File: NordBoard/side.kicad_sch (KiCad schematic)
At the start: 39 parts, among them SW15 SW_Push, SW16 SW_Push, SW2 SW_Push, SW22 SW_Push, SW23 SW_Push, SW24 SW_Push, SW25 SW_Push, SW26 SW_Push, SW27 SW_Push, SW28 SW_Push, SW29 SW_Push, SW30 SW_Push, SW31 SW_Push, SW32 SW_Push, SW33 SW_Push, SW34 SW_Push, SW9 SW_Push, U1 MOUDLE-SEEEDUINO-XIAO

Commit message: feat: finish schem, finish PCB layout
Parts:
- removed U1: MOUDLE-SEEEDUINO-XIAO, Seeed Studio XIAO Series Library:XIAO-RP2040-DIP, symbol XIAO_RP2040:MOUDLE-SEEEDUINO-XIAO
- added U2: Seeeduino Xiao rp2040, PCM_marbastlib-xp-promicroish:Xiao_rp2040_ACH, symbol PCM_marbastlib-promicroish:Seeeduino_Xiao_rp2040
- D1, D19, D20, D21, D22, D23, D24, D25, D26, D27, D28, D29, D30, D31, D32, D33, D34: footprint (none) -> Diode_SMD:D_SMA-SMB_Universal_Handsoldering
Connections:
- net COL0: now also U2.2 (P27)
- net COL1: now also U2.3 (P28)
- net COL2: now also U2.4 (P29)
- net COL3: now also SW30.1, U2.5 (P6)
- net COL4: now also U2.6 (P7)
- net GND: now also U2.9 (GND)
- net ROW0: now also U2.11 (P3)
- net ROW1: now also U2.12 (P4)
- net ROW2: now also U2.13 (P2)
- net ROW3: now also U2.14 (P1)
- no-connect marks 4 -> 10
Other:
- note added: "Matrix Left"
- note added: "Xiao"

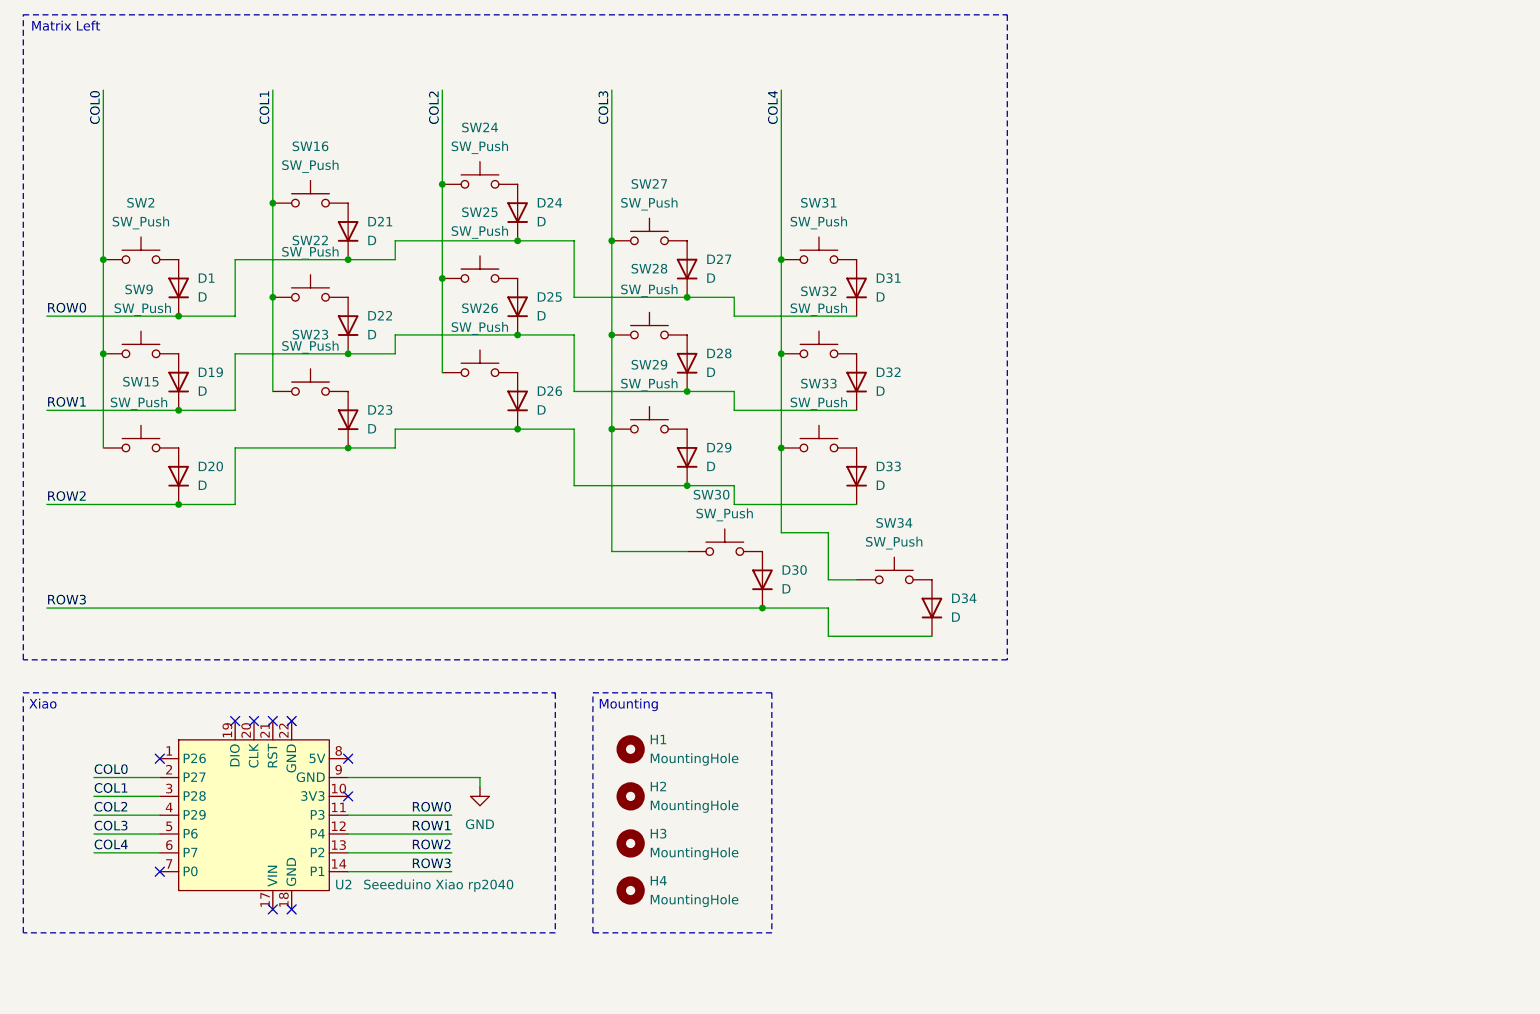
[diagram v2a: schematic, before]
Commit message: feat: new col in schem (not in PCB)
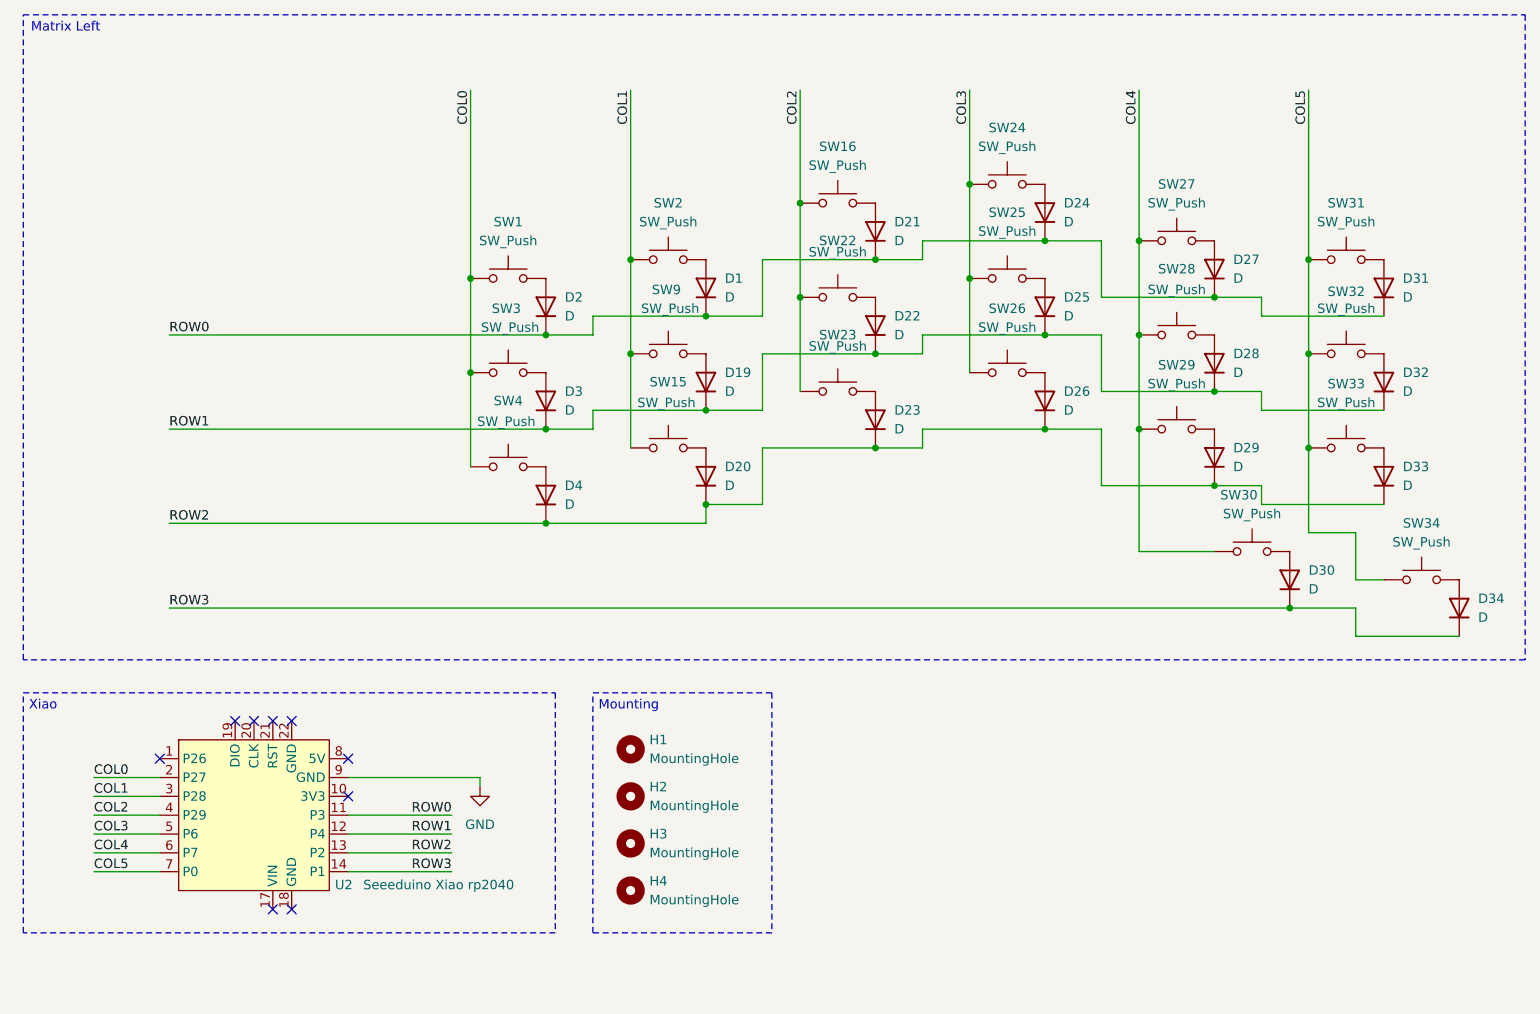
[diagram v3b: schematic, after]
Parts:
- added D2, D3, D4: D, Diode_SMD:D_SMA-SMB_Universal_Handsoldering, symbol Device:D
- added SW1, SW3, SW4: SW_Push, PCM_marbastlib-choc:SW_choc_v1_1u, symbol Switch:SW_Push
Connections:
- net COL0: now also SW1.1, SW3.1, SW4.1; no longer SW15.1, SW2.1, SW9.1
- net COL1: now also SW15.1, SW2.1, SW9.1; no longer SW16.1, SW22.1, SW23.1
- net COL2: now also SW16.1, SW22.1, SW23.1; no longer SW24.1, SW25.1, SW26.1
- net COL3: now also SW24.1, SW25.1, SW26.1; no longer SW27.1, SW28.1, SW29.1, SW30.1
- net COL4: now also SW27.1, SW28.1, SW29.1, SW30.1; no longer SW31.1, SW32.1, SW33.1, SW34.1
- net ROW0: now also D2.1 (K)
- net ROW1: now also D3.1 (K)
- net ROW2: now also D4.1 (K)
- net COL5: now reaches U2.7 (P0)
- net COL5: now also SW31.1, SW32.1, SW33.1, SW34.1
- new net: D3.2 (A), SW3.2
- new net: D4.2 (A), SW4.2
- new net: D2.2 (A), SW1.2
- no-connect marks 10 -> 9
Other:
- moved on the sheet: D1, D19, D20, D21, D22, D23, D24, D25, D26, D27, D28, D29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

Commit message: feat: revamp schem
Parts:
- removed U2: Seeeduino Xiao rp2040, PCM_marbastlib-xp-promicroish:Xiao_rp2040_ACH, symbol PCM_marbastlib-promicroish:Seeeduino_Xiao_rp2040
- added U1: XIAO-RP2040-DIP, Seeed Studio XIAO Series Library:XIAO-RP2040-DIP, symbol Seeed_Studio_XIAO_Series:XIAO-RP2040-DIP
- renumbered D2 to D1, D24 to D10, D25 to D11, D26 to D12, D27 to D13, D28 to D14, D29 to D15, D30 to D16, D31 to D17, D32 to D18, D33 to D19, D3 to D2, D34 to D20, D4 to D3, D1 to D4, D19 to D5, D20 to D6, D21 to D7, D22 to D8, D23 to D9, SW24 to SW10, SW25 to SW11, SW26 to SW12, SW27 to SW13, SW28 to SW14, SW29 to SW15, SW30 to SW16, SW31 to SW17, SW32 to SW18, SW33 to SW19, SW3 to SW2, SW34 to SW20, SW4 to SW3, SW2 to SW4, SW9 to SW5, SW15 to SW6, SW16 to SW7, SW22 to SW8, SW23 to SW9
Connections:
- net COL0: now also U1.2 (GPIO27/ADC1/A1)
- net COL1: now also U1.3 (GPIO28/ADC2/A2)
- net COL2: now also U1.4 (GPIO29/ADC3/A3)
- net COL3: now also U1.5 (GPIO6/SDA)
- net COL4: now also U1.6 (GPIO7/SCL)
- net COL5: now also U1.7 (GPIO0/TX)
- net GND: now also U1.13 (GND)
- net ROW0: now also U1.11 (GPIO3/MOSI)
- net ROW1: now also U1.10 (GPIO4/MISO)
- net ROW2: now also U1.9 (GPIO2/SCK)
- net ROW3: now also U1.8 (GPIO1/RX)
- no-connect marks 9 -> 3
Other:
- note added: "Matrix"
- note removed: "Matrix Left"
- moved on the sheet: D1, D10, D11, D12, D13, D14, D15, D16, D17, D18, D19, D2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

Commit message: chore: pcb board cleanup
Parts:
- removed H4: MountingHole, MountingHole:MountingHole_2.2mm_M2, symbol Mechanical:MountingHole
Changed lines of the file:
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@@
 	(rectangle
 		(start 101.6 110.49)
-		(end 125.73 142.875)
+		(end 125.73 135.89)
 		(stroke
 			(width 0)
@@
 				)
 				(path "/7cf7f72d-7ab1-4807-b592-339093d5ca44/a5832e99-b0f3-4441-a24d-2a862f25015f"
-					(reference "H5")
+					(reference "H4")
 					(unit 1)
 				)
@@
 	)
 	(symbol
-		(lib_id "Mechanical:MountingHole")
-		(at 106.68 137.16 0)
-		(unit 1)
-		(exclude_from_sim no)
-		(in_bom no)
-		(on_board yes)
-		(dnp no)
-		(fields_autoplaced yes)
-		(property "Reference" "H4"
-			(at 109.22 135.8899 0)
-			(effects
-				(font
-					(size 1.27 1.27)
-				)
-				(justify left)
-			)
-		)
-		(property "Value" "MountingHole"
-			(at 109.22 138.4299 0)
-			(effects
-				(font
-					(size 1.27 1.27)
-				)
-				(justify left)
-			)
-		)
-		(property "Footprint" "MountingHole:MountingHole_2.2mm_M2"
-			(at 106.68 137.16 0)
-			(effects
-				(font
-					(size 1.27 1.27)
-				)
-				(hide yes)
-			)
-		)
-		(property "Datasheet" "~"
-			(at 106.68 137.16 0)
-			(effects
-				(font
-					(size 1.27 1.27)
-				)
-				(hide yes)
-			)
-		)
-		(property "Description" "Mounting Hole without connection"
-			(at 106.68 137.16 0)
-			(effects
-				(font
-					(size 1.27 1.27)
-				)
-				(hide yes)
-			)
-		)
-		(instances
-			(project "NordBoard"
-				(path "/7cf7f72d-7ab1-4807-b592-339093d5ca44/7e48f610-41a3-4552-82fa-dd005ce074be"
-					(reference "H4")
-					(unit 1)
-				)
-				(path "/7cf7f72d-7ab1-4807-b592-339093d5ca44/a5832e99-b0f3-4441-a24d-2a862f25015f"
-					(reference "H8")
-					(unit 1)
-				)
-			)
-		)
-	)
-	(symbol
 		(lib_id "Switch:SW_Push")
 		(at 162.56 88.9 0)
@@
 				)
 				(path "/7cf7f72d-7ab1-4807-b592-339093d5ca44/a5832e99-b0f3-4441-a24d-2a862f25015f"
-					(reference "H6")
+					(reference "H5")
 					(unit 1)
 				)
@@
 				)
 				(path "/7cf7f72d-7ab1-4807-b592-339093d5ca44/a5832e99-b0f3-4441-a24d-2a862f25015f"
-					(reference "H7")
+					(reference "H6")
 					(unit 1)
 				)

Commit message: fix: fix pcb errors
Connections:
- net GND: no longer names the net of U1.13 (GND)
- no-connect marks 3 -> 4
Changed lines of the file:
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@@
 		(at 74.93 129.54)
 	)
+	(no_connect
+		(at 74.93 125.73)
+	)
 	(wire
 		(pts
@@
 	(wire
 		(pts
-			(xy 74.93 125.73) (xy 92.71 125.73)
-		)
-		(stroke
-			(width 0)
-			(type default)
-		)
-	)
-	(wire
-		(pts
 			(xy 142.24 80.01) (xy 157.48 80.01)
 		)
@@
 		(pts
 			(xy 74.93 144.78) (xy 88.9 144.78)
-		)
-		(stroke
-			(width 0)
-			(type default)
-		)
-	)
-	(wire
-		(pts
-			(xy 92.71 125.73) (xy 92.71 127)
 		)
 		(stroke
@@
 					(unit 1)
 				)
-			)
-		)
-	)
-	(symbol
-		(lib_id "power:GND")
-		(at 92.71 127 0)
-		(unit 1)
-		(exclude_from_sim no)
-		(in_bom yes)
-		(on_board yes)
-		(dnp no)
-		(fields_autoplaced yes)
-		(property "Reference" "#PWR03"
-			(at 92.71 133.35 0)
-			(effects
-				(font
-					(size 1.27 1.27)
-				)
-				(hide yes)
-			)
-		)
-		(property "Value" "GND"
-			(at 92.71 132.08 0)
-			(effects
-				(font
-					(size 1.27 1.27)
-				)
-			)
-		)
-		(property "Footprint" ""
-			(at 92.71 127 0)
-			(effects
-				(font
-					(size 1.27 1.27)
-				)
-				(hide yes)
-			)
-		)
-		(property "Datasheet" ""
-			(at 92.71 127 0)
-			(effects
-				(font
-					(size 1.27 1.27)
-				)
-				(hide yes)
-			)
-		)
-		(property "Description" "Power symbol creates a global label with name \"GND\" , ground"
-			(at 92.71 127 0)
-			(effects
-				(font
-					(size 1.27 1.27)
-				)
-				(hide yes)
-			)
-		)
-		(pin "1"
-		)
-		(instances
-			(project "NordBoard"
-				(path "/7cf7f72d-7ab1-4807-b592-339093d5ca44/7e48f610-41a3-4552-82fa-dd005ce074be"
-					(reference "#PWR03")
-					(unit 1)
-				)
-				(path "/7cf7f72d-7ab1-4807-b592-339093d5ca44/a5832e99-b0f3-4441-a24d-2a862f25015f"
-					(reference "#PWR04")
-					(unit 1)
-				)
